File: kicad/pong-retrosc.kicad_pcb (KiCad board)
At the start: 2 copper layers, 100 x 60 mm, 24 parts, among them J1 RCA video (na placa), J4 chave A/B (painel), J5 pot P1 (painel), J6 pot P2 (painel), J7 START (painel), J8 RCA audio L (na placa), J9 RCA audio R (na placa), U1 RaspberryPi_Pico, U2 PAM8403 HW-012

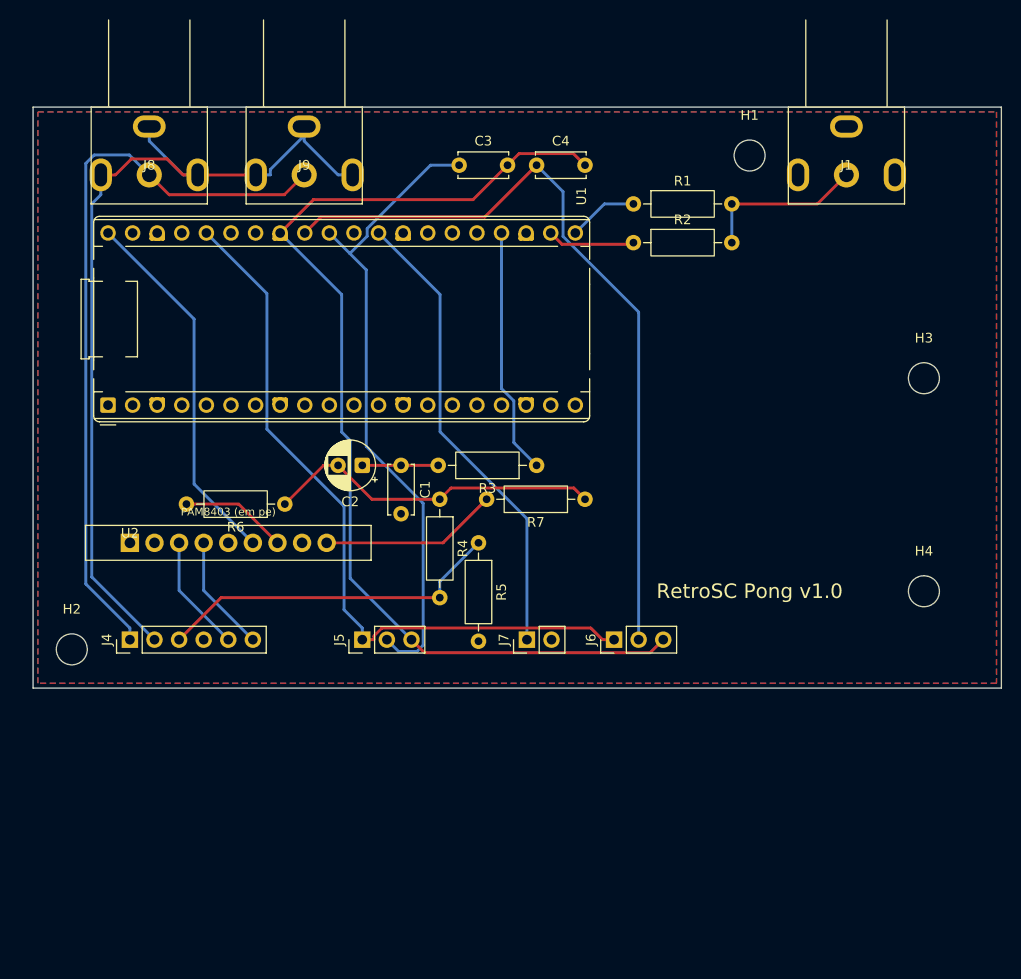
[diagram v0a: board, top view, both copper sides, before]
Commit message: kicad: placa 55x88 refeita com feedback de revisao (DRC 0 erros)
- PAM8403: barra real de 11 posicoes (4+vazio+2+vazio+3), corpo na placa
  ao lado do USB e pot de volume saindo pela borda superior
- Pico com o USB colado na borda para facilitar o cabo no gabinete
- RCAs com o barril protraindo ~8,5 mm para fora da borda direita
- headers empilhados com nome e funcao de cada pino no silk; J5+J6 na
  mesma fileira com 1 vaga (aceita conector femea 1x7 unico)
- furos M3 regulares: base H2/H4/H3 em y84 (H2-H3 = 45 mm, H4 central)
  e H1 no eixo, 45 mm acima de H4
- logo RetroSC no silk da frente, entre as fileiras do Pico (0,22 mm/px)
- gerbers + pong-retrosc-gerbers.zip prontos para a fabrica

Co-Authored-By: Claude Opus 4.8 <noreply@anthropic.com>
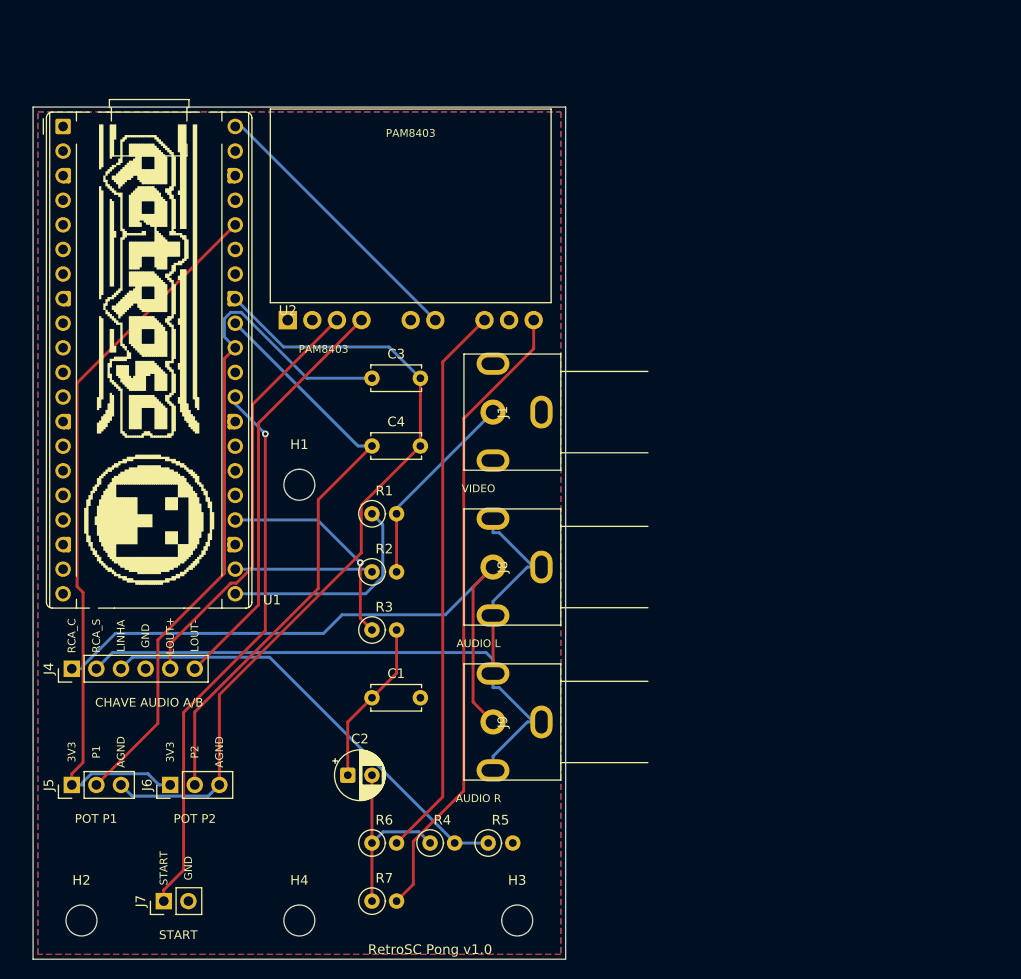
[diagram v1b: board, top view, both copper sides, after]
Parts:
- R1, R2, R3, R4, R5, R6, R7: footprint R_Axial_DIN0207_L6.3mm_D2.5mm_P10.16mm_Horizontal -> R_Axial_DIN0207_L6.3mm_D2.5mm_P2.54mm_Vertical
- moved H4 72.9 mm to (47.5, 104.0)
- moved H3 70.0 mm to (70.0, 104.0)
- moved J9 59.8 mm to (67.5, 83.5), turned to -90 degrees
- moved H1 57.6 mm to (47.5, 59.0)
- moved J8 53.9 mm to (67.5, 67.5), turned to -90 degrees
- moved J6 48.2 mm to (34.2, 90.0)
- moved R7 47.0 mm to (55.0, 102.0), turned to 0 degrees
- moved J7 46.2 mm to (33.5, 102.0)
- moved J1 44.0 mm to (67.5, 51.5), turned to -90 degrees
- moved R2 43.4 mm to (55.0, 68.0)
- moved R1 41.9 mm to (55.0, 62.0)
- moved R6 36.1 mm to (55.0, 96.0), turned to 0 degrees
- moved R4 35.5 mm to (61.0, 96.0), turned to 0 degrees
- moved C4 33.6 mm to (55.0, 55.0)
- moved J5 33.5 mm to (24.0, 90.0)
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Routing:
- net AMP_R: track 18.4 -> 65.9 mm
- net AMP_L: track 11.1 -> 57.8 mm
- net LOUT_P: track 12.1 -> 43.5 mm
- net LOUT_N: track 12.1 -> 43.1 mm
- net AGND: track 110.1 -> 84.2 mm
- net POT2: track 80.2 -> 62.0 mm
- net SYNC: track 7.24 -> 22.9 mm
- net AUD_C: track 35.1 -> 20.0 mm
- net RCA_S: track 91.3 -> 79.5 mm
- net RCA_C: track 76.5 -> 65.7 mm
- net LINHA: track 36.0 -> 46.4 mm
- net START: track 48.3 -> 57.7 mm, vias 0 -> 1
- net +5V: track 38.2 -> 28.9 mm
- net AUD_F: track 7.84 -> 17.1 mm
- net POT1: track 66.6 -> 72.9 mm
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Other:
- board size 100 x 60 mm -> 55 x 88 mm
- board text added: "3V3"
- board text added: "AGND"
- board text added: "AUDIO L"
- board text added: "AUDIO R"
- board text added: "CHAVE AUDIO A/B"
- board text added: "GND"
- board text added: "LINHA"
- board text added: "LOUT+"
- board text added: "LOUT-"
- board text added: "P1"
- board text added: "P2"
- board text added: "PAM8403"
- board text added: "POT P1"
- board text added: "POT P2"
- board text added: "RCA_C"
- board text added: "RCA_S"
- board text added: "START"
- board text added: "VIDEO"

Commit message: kicad: variante para o RP2040 roxo + pinagem dos 3 modulos
Os clones do Pico tem a MESMA furacao mas outra funcao em cada posicao
de pino, entao o pipeline passa a gerar duas placas (--yd nos scripts):

- oficial (pong-retrosc): Raspberry Pi Pico e tambem a YD-RP2040 de 3
  botoes, cuja pinagem coincide em todas as posicoes que o projeto usa
- roxa 1 botao (pong-retrosc-yd): SYNC/VIDEO/AUDIO em 19/20/21, START em
  25, pots em 30/31, AGND em 29 e GND so em 6/15/35/38

Detalhes:
- a variante usa simbolo de conector 2x20 no lugar do simbolo do Pico:
  este une os pinos de mesmo nome (os 8 GND), o que amarraria GPIOs da
  roxa ao plano de terra
- marcas GP17/GP18 no silk das duas placas para conferir, antes de
  soldar, se placa e modulo sao da mesma variante
- docs/pinout.md com a pinagem completa dos 3 modulos lado a lado e as
  ressalvas da YD de 3 botoes (GP23=WS2812, pino 40 = Vout)
- tools/dsn_tweak.py versionado: a roxa precisa de trilha 0,25 mm no
  roteamento (com 0,30 o net START nao fecha)

DRC 0 erros e 0 desconectados nas duas placas; gerbers + zip de cada uma.

Co-Authored-By: Claude Opus 4.8 <noreply@anthropic.com>
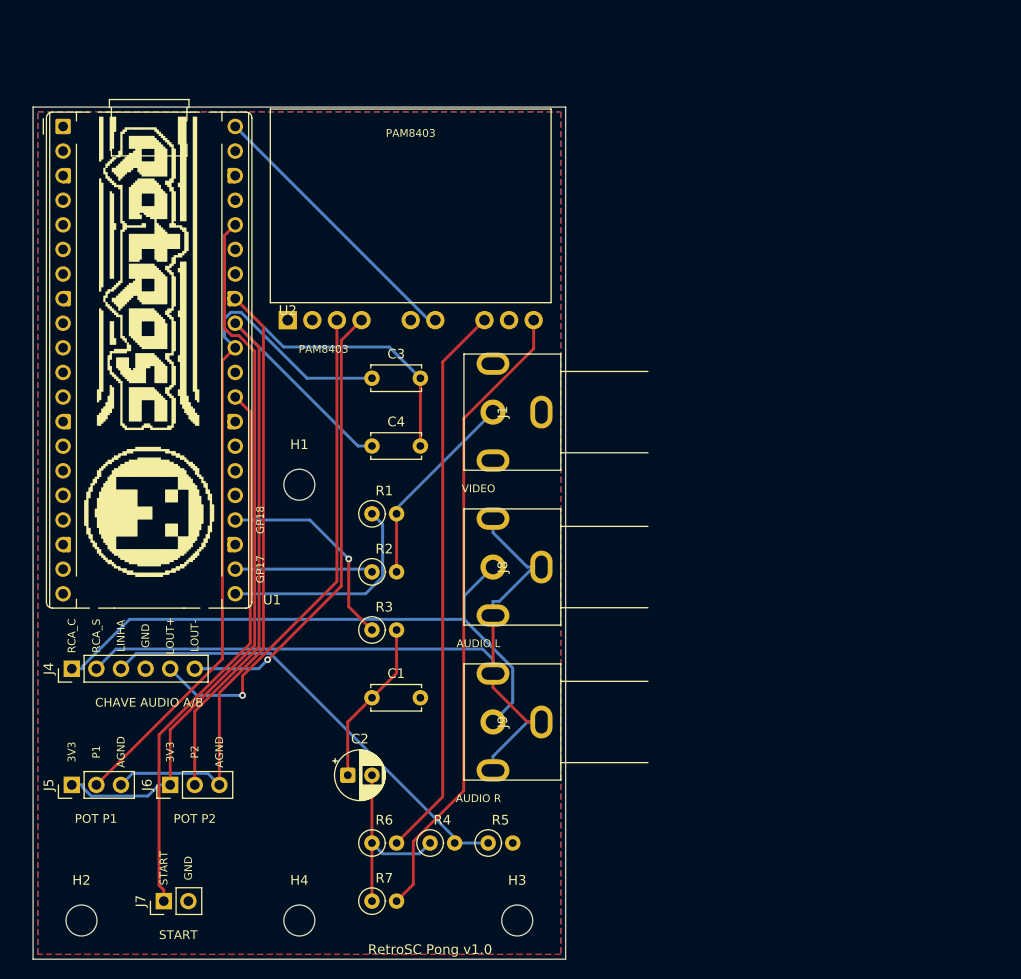
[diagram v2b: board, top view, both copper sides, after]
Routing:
- net AGND: track 84.2 -> 94.0 mm
- net POT2: track 62.0 -> 70.8 mm
- net LOUT_P: track 43.5 -> 51.4 mm, vias 0 -> 1
- net LOUT_N: track 43.1 -> 47.0 mm, vias 0 -> 1
- net RCA_C: track 65.7 -> 63.0 mm
- net +3V3: track 76.6 -> 74.9 mm
- net RCA_S: track 79.5 -> 80.6 mm
- net START: track 57.7 -> 56.8 mm, vias 1 -> 0
- net LINHA: track 46.4 -> 47.0 mm
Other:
- board text added: "GP17"
- board text added: "GP18"

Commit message: kicad: placa 80x66 para a caixa Patola PB-085/3 (DRC 0 erros)
A placa era 55 x 88 e nao entrava na caixa. Agora e 80 x 66, contra os
~82 x 70 internos da PB-085/3 (85 x 73 x 32 montada).

Furacao refeita para os bossos da TAMPA: eram 4 furos M3 em losango de
45 mm; agora sao 2 furos a 58 mm entre centros, na linha de centro da
largura -- que e o que a caixa oferece (2 bossos com furo-guia o2,5, a
58 mm, no meio do lado de 85 mm). Em troca, o miolo das bordas de cima e
de baixo (x 36,5..43,5) virou area reservada.

Rearranjo, ja que a placa deitou (80 no maior lado):
- Pico a esquerda, USB na borda de cima; PAM8403 no topo a direita, com o
  pot saindo pela mesma borda
- os 3 RCAs desceram para a borda direita abaixo do amp
- os headers de painel foram para UMA fileira na borda de baixo (duas nao
  cabem: cada uma precisa de ~9 mm com os rotulos de funcao)
- rotulos dos headers centralizados sobre cada conector (PCB_TEXT e
  centrado na coordenada -- antes "CHAVE AUDIO A/B" saia cortado)

As duas variantes roteiam com 0 erros e 0 desconectados; gerbers, ZIPs e
imagens regenerados. Docs atualizados com as dimensoes, a furacao e o
aviso de que RCAs, pot e USB atravessam as paredes da caixa.

Co-Authored-By: Claude Opus 5 <noreply@anthropic.com>
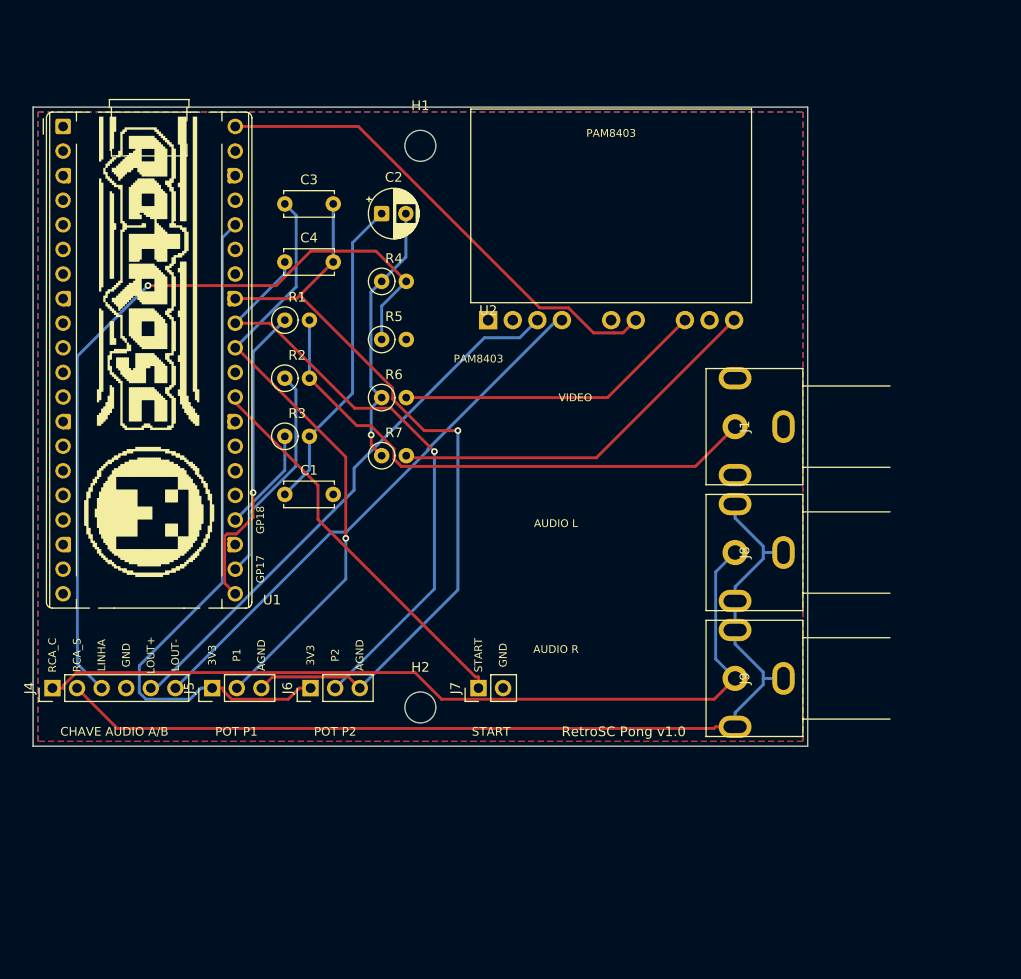
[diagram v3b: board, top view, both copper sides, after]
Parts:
- removed H3, H4: MountingHole_3.2mm_M3, MountingHole_3.2mm_M3
- moved R4 58.2 mm to (56.0, 38.0)
- moved C2 58.1 mm to (56.0, 31.0)
- moved R5 53.2 mm to (56.0, 44.0)
- moved R6 46.0 mm to (56.0, 50.0)
- moved R7 46.0 mm to (56.0, 56.0)
- moved H2 41.3 mm to (60.0, 82.0)
- moved J7 39.2 mm to (66.0, 80.0)
- moved H1 37.2 mm to (60.0, 24.0)
- moved J9 25.4 mm to (92.5, 79.0)
- moved J1 25.0 mm to (92.5, 53.0)
- moved J8 25.0 mm to (92.5, 66.0)
- moved C1 22.8 mm to (46.0, 60.0)
- moved R1 21.9 mm to (46.0, 42.0)
- moved R2 21.9 mm to (46.0, 48.0)
- moved R3 21.9 mm to (46.0, 54.0)
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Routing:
- net COMPOSITE: track 20.6 -> 56.1 mm
- net LINHA: track 47.0 -> 82.1 mm, vias 0 -> 1
- net AMP_R: track 65.9 -> 39.8 mm
- net AMP_L: track 57.8 -> 32.1 mm
- net RCA_C: track 63.0 -> 88.0 mm
- net +5V: track 28.9 -> 50.7 mm
- net RCA_S: track 80.6 -> 101.8 mm
- net START: track 56.8 -> 40.6 mm
- net AUD_F: track 17.1 -> 33.1 mm
- net AGND: track 94.0 -> 82.3 mm, vias 0 -> 1
- net AUDIO_PWM: track 21.7 -> 10.8 mm, vias 1 -> 0
- net POT1: track 72.9 -> 62.6 mm, vias 0 -> 1
- net SYNC: track 22.9 -> 31.9 mm, vias 0 -> 1
- net LOUT_N: track 47.0 -> 55.7 mm, vias 1 -> 0
- net VIDEO: track 14.2 -> 22.8 mm
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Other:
- board size 55 x 88 mm -> 80 x 66 mm

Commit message: kicad: cobre longe dos parafusos e serigrafia corrigida
Dois problemas apontados na revisao da placa.

1. Trilhas rentes aos furos de montagem: o roteador passava sinal a 2,0 mm
   do centro do furo -- 0,4 mm da borda, debaixo da cabeca do parafuso.
   Agora cada furo tem uma AREA DE EXCLUSAO de raio 3,6 mm (rule area nas
   2 faces) barrando trilha e via; o plano de GND continua entrando, que
   encostar em GND e inofensivo. A trilha mais proxima passou de 2,0 para
   3,9 mm. make_decoy.py preserva as rule areas (antes removia todas as
   zonas, e o roteador nao as via).

2. Serigrafia:
   - GP17/GP18 nao diziam QUAL pino, ao lado de 20 pads iguais: agora tem
     linha de chamada ate o pad, comecando fora do contorno do modulo
   - VIDEO/AUDIO L/AUDIO R estavam soltos no meio da placa, a 17 mm dos
     jacks: foram para junto de cada um, com a referencia (ex.: "VIDEO (J1)")
   - referencias que caiam sobre pads (J1/J4..J9, H1/H2, U2) ocultadas ou
     movidas -- a informacao esta nos rotulos descritivos
   - contorno do footprint do RCA cruzava as proprias abas de terra: as
     laterais agora sao quebradas na altura dos pads
   - logo reescalado (0,22 -> 0,19 mm/px) para caber ENTRE as duas linhas
     verticais do footprint do Pico, que ele atravessava
   - texto de versao foi para a area livre do meio (o da variante YD nao
     cabia no rodape)

   silk_over_copper 11 -> 0, silk_overlap 30 -> 0. Sobram 12 avisos de
   borda: USB e barris dos RCAs cruzando o contorno, que e intencional.

Na variante YD o roteador agora recebe 0,17 mm de isolamento: pedindo os
0,15 do projeto ele entregava 0,1478 e o DRC reprovava.

DRC: 0 erros nas duas placas. Gerbers, ZIPs, renders e desenho de encaixe
regenerados.

Co-Authored-By: Claude Opus 5 <noreply@anthropic.com>
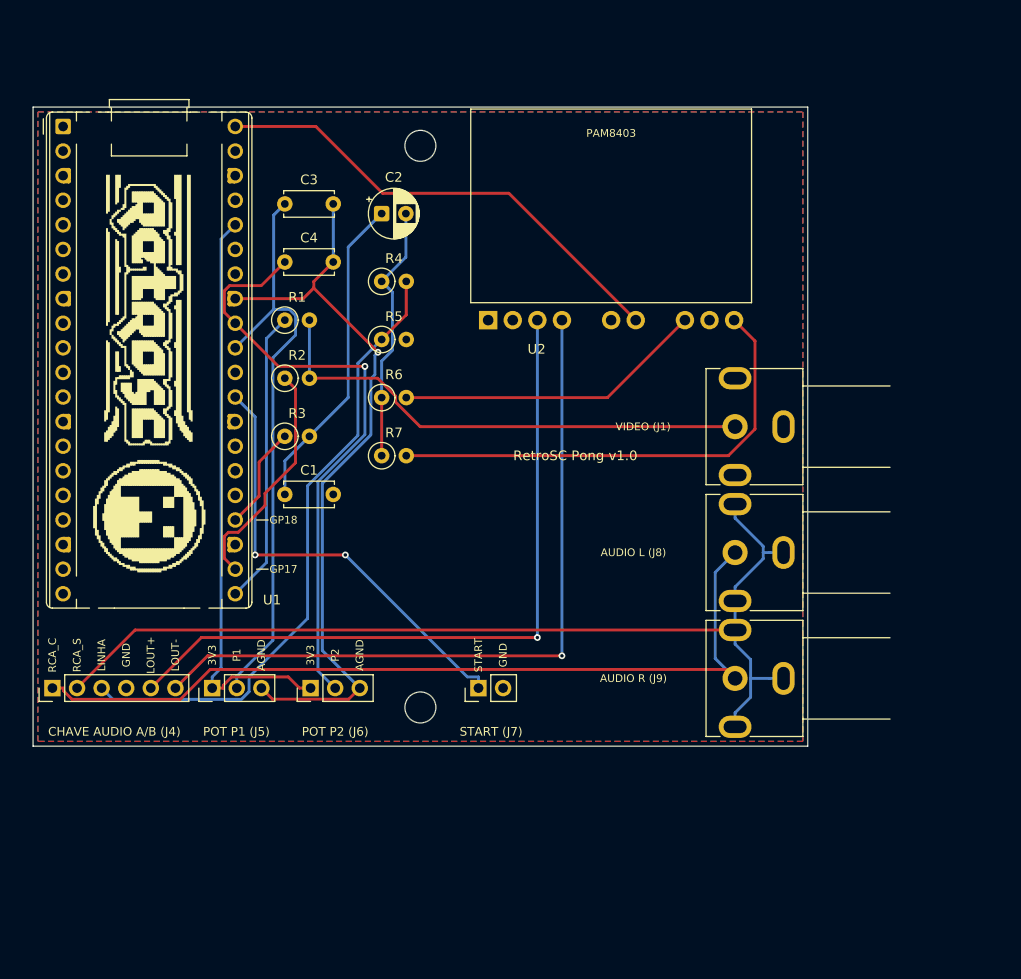
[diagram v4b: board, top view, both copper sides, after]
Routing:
- net LOUT_N: track 55.7 -> 76.0 mm, vias 0 -> 1
- net LOUT_P: track 57.0 -> 74.9 mm, vias 0 -> 1
- net LINHA: track 82.1 -> 65.1 mm, vias 1 -> 0
- net +3V3: track 72.0 -> 60.1 mm
- net AMP_R: track 39.8 -> 49.3 mm
- net START: track 40.6 -> 46.6 mm, vias 0 -> 2
- net AGND: track 82.3 -> 77.2 mm
- net COMPOSITE: track 56.1 -> 52.4 mm
- net POT1: track 62.6 -> 60.5 mm, vias 1 -> 0
- net VIDEO: track 22.8 -> 24.3 mm
- net SYNC: track 31.9 -> 30.4 mm, vias 1 -> 0
- net +5V: track 50.7 -> 49.6 mm
- net RCA_S: track 101.8 -> 102.7 mm
- net AUD_C: track 27.8 -> 27.0 mm, vias 1 -> 0
- net POT2: track 63.2 -> 62.5 mm
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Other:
- board text added: "AUDIO L (J8)"
- board text added: "AUDIO R (J9)"
- board text added: "CHAVE AUDIO A/B (J4)"
- board text added: "POT P1 (J5)"
- board text added: "POT P2 (J6)"
- board text added: "START (J7)"
- board text added: "VIDEO (J1)"
- board text removed: "AUDIO L"
- board text removed: "AUDIO R"
- board text removed: "CHAVE AUDIO A/B"
- board text removed: "PAM8403"
- board text removed: "POT P1"
- board text removed: "POT P2"
- board text removed: "VIDEO"
